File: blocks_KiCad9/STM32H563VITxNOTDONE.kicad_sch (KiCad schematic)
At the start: 22 parts

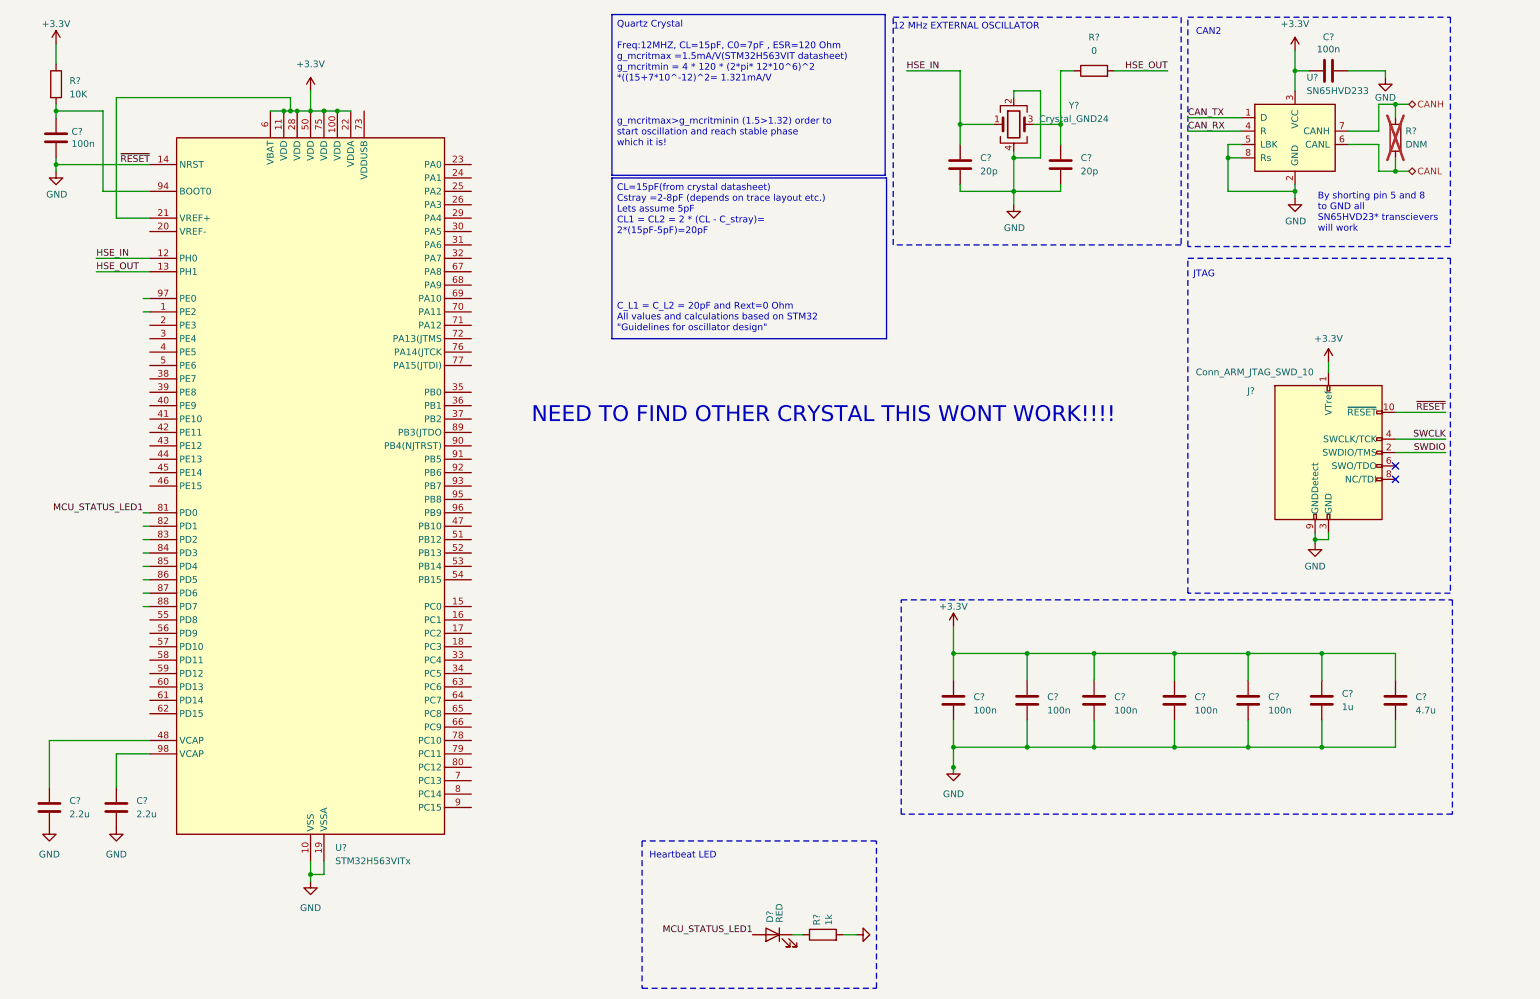
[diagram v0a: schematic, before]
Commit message: Update on the STM32H563VITx
Only thing left is double checking the hardware watchdog since we ordered different ones.
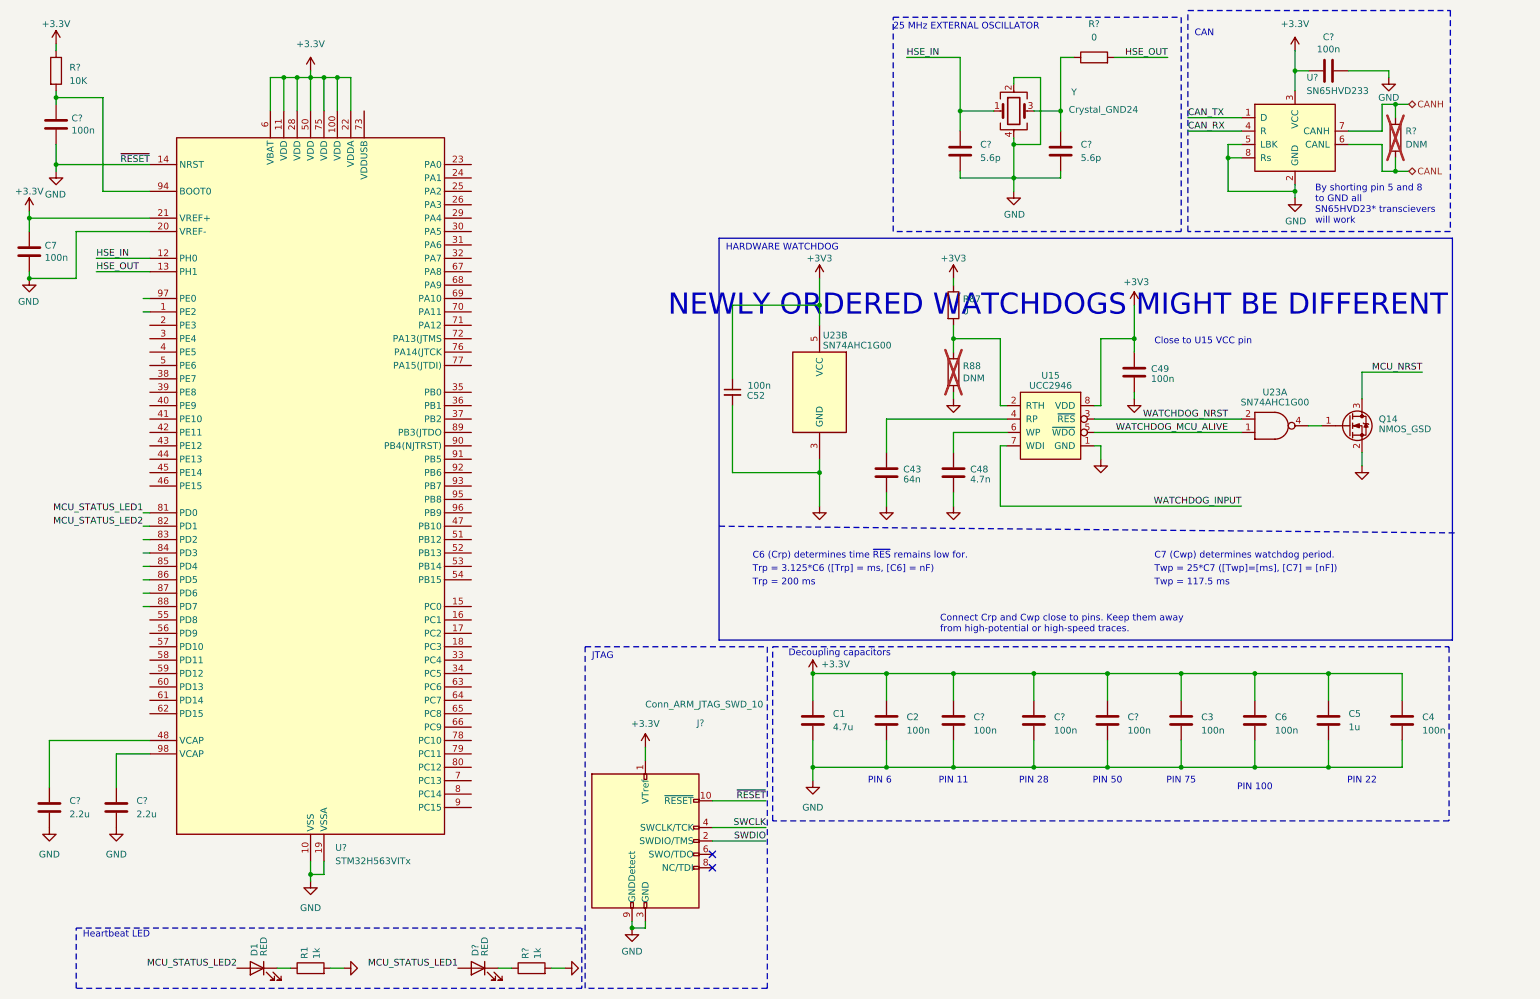
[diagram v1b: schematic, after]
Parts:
- removed C?: 4.7u, Capacitor_SMD:C_1210_3225Metric, symbol Device:C
- removed C?: 1u, Capacitor_SMD:C_1210_3225Metric, symbol Device:C
- removed C? (x2): 100n, Capacitor_SMD:C_0603_1608Metric, symbol Device:C
- added C1: 4.7u, Capacitor_SMD:C_0603_1608Metric, symbol Device:C
- added C2, C3, C4, C49, C6, C7: 100n, Capacitor_SMD:C_0603_1608Metric, symbol Device:C
- added C43: 64n, Capacitor_SMD:C_0603_1608Metric, symbol Device:C
- added C48: 4.7n, Capacitor_SMD:C_0603_1608Metric, symbol Device:C
- added C5: 1u, Capacitor_SMD:C_1210_3225Metric, symbol Device:C
- added C52: 100n, Capacitor_SMD:C_0603_1608Metric, symbol Device:C_Small
- added D1: RED, LED_SMD:LED_0603_1608Metric, symbol Device:LED
- added Q14: NMOS_GSD, Package_TO_SOT_SMD:SOT-23, symbol Device:Q_NMOS_GSD
- added R1: 1k, Resistor_SMD:R_0603_1608Metric, symbol Device:R
- added R87: 0, Resistor_SMD:R_0603_1608Metric, symbol Device:R
- added R88: DNM, Resistor_SMD:R_0603_1608Metric, symbol Device:R
- added U15: UCC2946, Package_SO:SOIC-8_3.9x4.9mm_P1.27mm, symbol DeV18-AMS_bot_0.1-rescue:UCC2946-KTHFS
- added U23: SN74AHC1G00, Package_TO_SOT_SMD:SOT-23-5, symbol KTHFS:SN74AHC1G00
- C? (x2): value 20p -> 5.6p
- gave numbers to parts that had none: 1
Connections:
- net +3.3V: now also C1.1, C2.1, C3.1, C4.1, C5.1, C6.1, C7.1
- net GND: now also U?.20 (VREF-), C1.2, C2.2, C3.2, C4.2, C43.2, C48.2, C49.2, C5.2, C52.2, C6.2, C7.2, Q14.2 (S), R1.2, R88.2, U15.1 (GND), U23.3 (GND)
- net MCU_STATUS_LED2: now reaches U?.82 (PD1)
- net MCU_STATUS_LED2: now also D1.2 (A)
- new net: R87.2, R88.1, U15.2 (RTH)
- new net: C43.1, U15.4 (RP)
- new net: C48.1, U15.6 (WP)
- new net: D1.1 (K), R1.1
- new net: Q14.1 (G), U23.4
- new net +3V3: C49.1, C52.1, R87.1, U15.8 (VDD), U23.5 (VCC)
- new net MCU_NRST: Q14.3 (D)
- new net WATCHDOG_INPUT: U15.7 (WDI)
- new net WATCHDOG_MCU_ALIVE: U15.5 (~{WDO}), U23.1
- new net WATCHDOG_NRST: U15.3 (~{RES}), U23.2
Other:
- note added: "25 MHz EXTERNAL OSCILLATOR"
- note added: "C6 (Crp) determines time ~{RES} remains low for."
- note added: "C7 (Cwp) determines watchdog period."
- note added: "CAN"
- note added: "Close to U15 VCC pin"
- note added: "Connect Crp and Cwp close to pins. Keep them away from high-potential or high-speed traces."
- note added: "Decoupling capacitors"
- note added: "HARDWARE WATCHDOG"
- note added: "NEWLY ORDERED WATCHDOGS MIGHT BE DIFFERENT"
- note added: "PIN 100"
- note added: "PIN 11"
- note added: "PIN 22"
- note added: "PIN 28"
- note added: "PIN 50"
- note added: "PIN 6"
- note added: "PIN 75"
- note added: "Trp = 200 ms"
- note added: "Trp = 3.125*C6 ([Trp] = ms, [C6] = nF)"
- note added: "Twp = 117.5 ms"
- note added: "Twp = 25*C7 ([Twp]=[ms], [C7] = [nF])"
- note removed: "12 MHz EXTERNAL OSCILLATOR"
- note removed: "CAN2"
- note removed: "NEED TO FIND OTHER CRYSTAL THIS WONT WORK!!!!"
- moved on the sheet: C?, D?, J?, R?, Y

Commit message: minor changes to mcu block
oscillator footprint and some other smaller changes for labels.
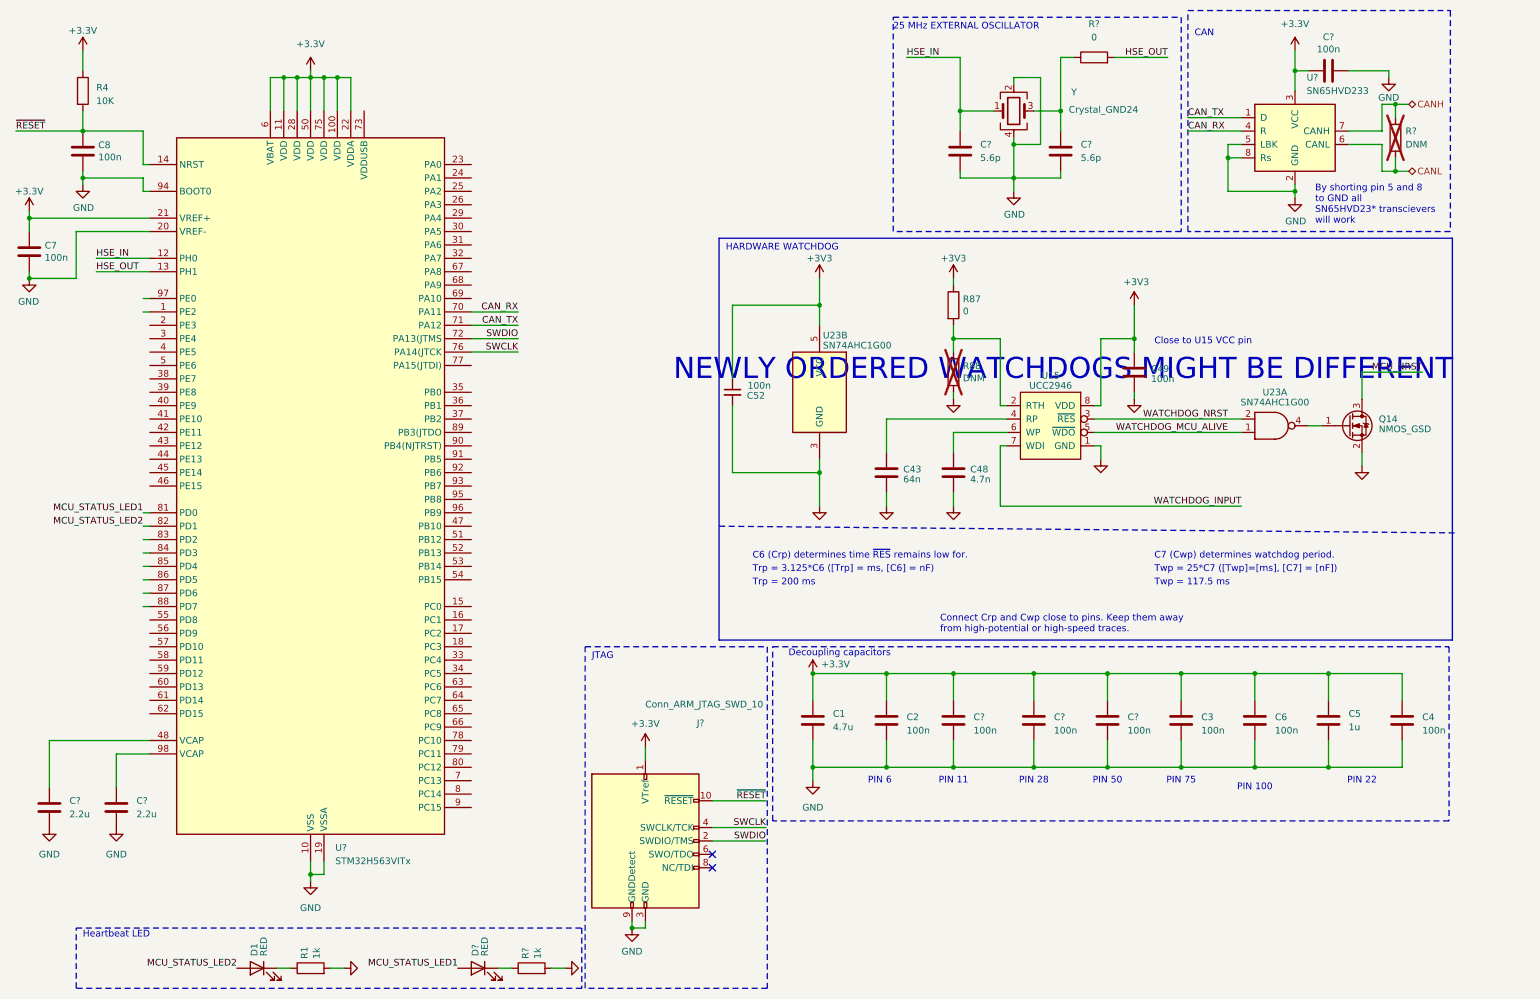
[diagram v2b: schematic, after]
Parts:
- removed C?: 100n, Capacitor_SMD:C_0603_1608Metric, symbol Device:C
- added C8: 100n, Capacitor_SMD:C_0603_1608Metric, symbol Device:C
- Y: footprint Crystal:Crystal_SMD_3225-4Pin_3.2x2.5mm_HandSoldering -> Crystal:Crystal_SMD_2016-4Pin_2.0x1.6mm
- gave numbers to parts that had none: 1
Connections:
- net CAN_RX: now also U?.70 (PA11)
- net CAN_TX: now also U?.71 (PA12)
- net GND: now also U?.94 (BOOT0), C8.2; no longer J?.10 (~{RESET}), U?.14 (NRST)
- net SWCLK: now also U?.76 (PA14(JTCK)
- net SWDIO: now also U?.72 (PA13(JTMS)
- net ~{RESET}: now reaches R4.2
- net ~{RESET}: now also J?.10 (~{RESET}), U?.14 (NRST), C8.1; no longer U?.94 (BOOT0)
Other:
- moved on the sheet: R4
